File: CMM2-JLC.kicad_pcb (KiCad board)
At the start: 4 copper layers, 130 x 102 mm, 111 parts, among them J1 Nunchuck, J2 VGA, J3 EXTERNAL I/O, J4 USB_C_Receptacle_USB2.0, J5 Audio, J6 USB A Host, J7 SWD, J8 Micro_SD_Card_Det, J9 Boot select, SW1 Reset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

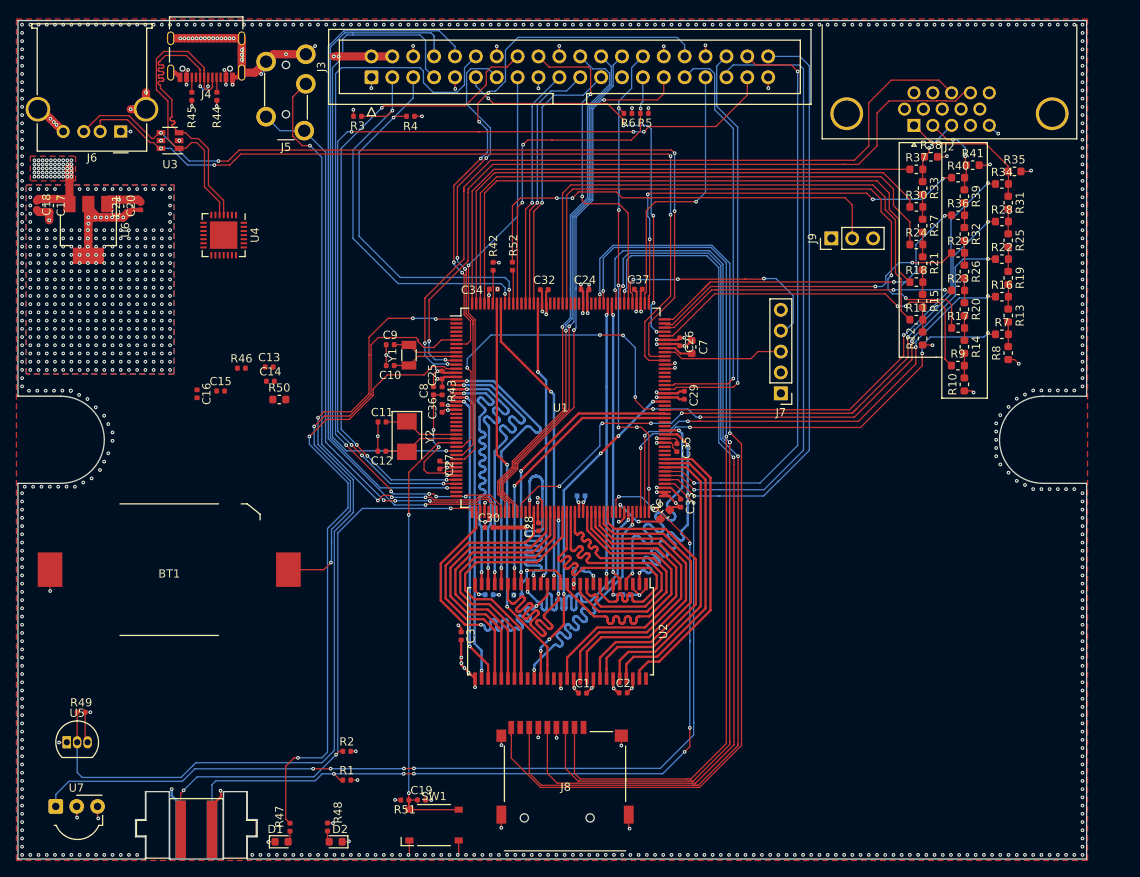
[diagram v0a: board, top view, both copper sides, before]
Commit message: Routed USB, UART and reset pins
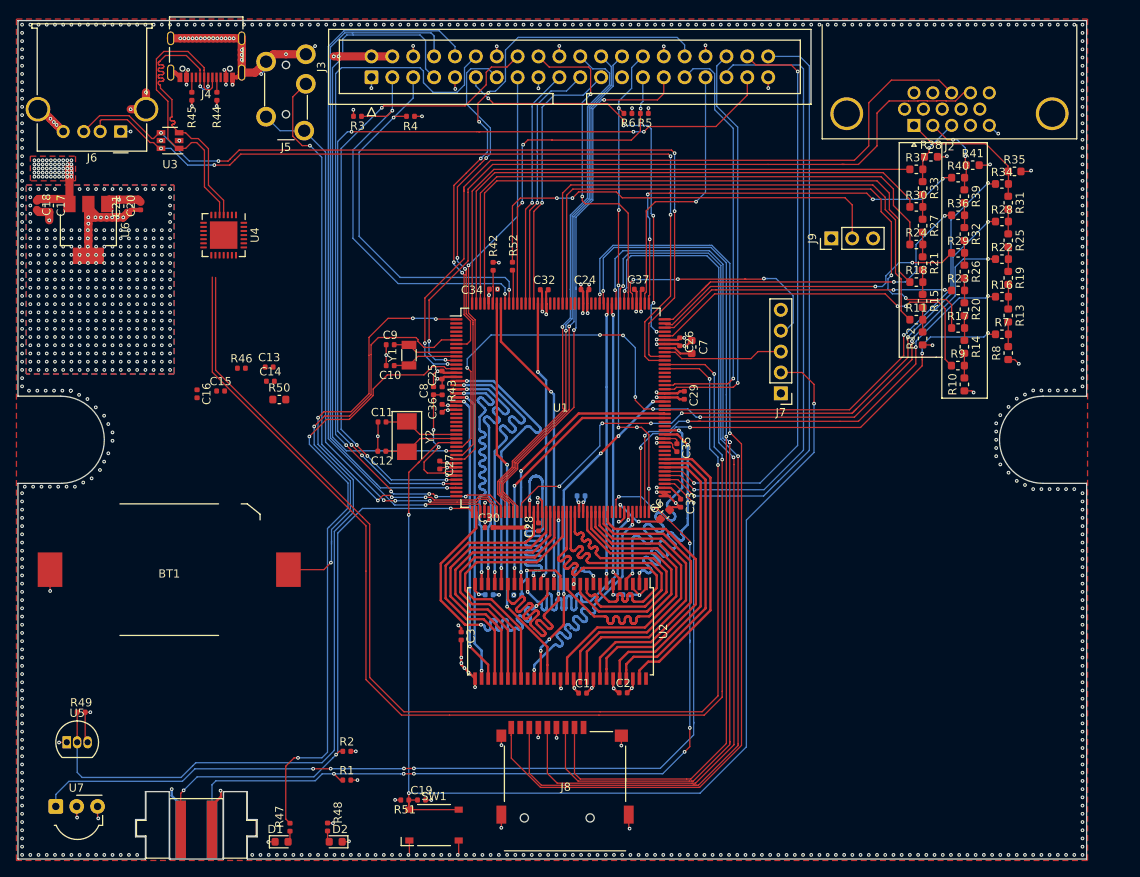
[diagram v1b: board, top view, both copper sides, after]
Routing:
- net /PA10: track 1.32 -> 149.0 mm, vias 1 -> 2
- net /PA9: track 1.30 -> 146.3 mm, vias 1 -> 2
- net /RESET: track 56.5 -> 152.2 mm, vias 2 -> 3
- net /PI1: track 43.9 -> 43.2 mm
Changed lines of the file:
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@@
     (thickness 1.6)
     (drawings 44)
-    (tracks 5255)
+    (tracks 5295)
     (zones 0)
     (modules 111)
@@
   (segment (start 133.552998 61.976) (end 132.788499 61.211501) (width 0.127) (layer F.Cu) (net 24))
   (segment (start 133.552999 61.976) (end 133.552998 61.976) (width 0.127) (layer F.Cu) (net 24))
-  (segment (start 132.788499 61.211501) (end 132.75 61.173001) (width 0.127) (layer F.Cu) (net 24))
   (segment (start 128.48851 54.26149) (end 128 54.75) (width 0.127) (layer F.Cu) (net 24))
   (segment (start 128 54.75) (end 127 54.75) (width 0.127) (layer B.Cu) (net 24))
@@
   (segment (start 127.95 51.8) (end 127.3 51.8) (width 0.127) (layer B.Cu) (net 107))
   (segment (start 129.25 50.5) (end 127.95 51.8) (width 0.127) (layer B.Cu) (net 107))
-  (segment (start 127.95 51.8) (end 127.5 52.25) (width 0.127) (layer B.Cu) (net 107))
   (segment (start 103.640776 52.390776) (end 103.785562 52.24599) (width 0.127) (layer F.Cu) (net 107))
   (segment (start 103.240776 52.790776) (end 103.640776 52.390776) (width 0.127) (layer F.Cu) (net 107))
@@
   (segment (start 73.612 115.997) (end 67.612 115.997) (width 0.127) (layer F.Cu) (net 148))
   (segment (start 71.144 71.35) (end 73.325 71.35) (width 0.127) (layer F.Cu) (net 148))
-  (segment (start 67.541 74.953) (end 71.144 71.35) (width 0.127) (layer F.Cu) (net 148))
   (segment (start 67.541 115.926) (end 67.612 115.997) (width 0.127) (layer F.Cu) (net 148))
   (segment (start 67.541 80.1219) (end 67.5386 80.1243) (width 0.127) (layer F.Cu) (net 148))
@@
   (segment (start 67.5386 80.1243) (end 67.5386 113.9825) (width 0.127) (layer B.Cu) (net 148))
   (segment (start 67.541 113.9849) (end 67.541 115.926) (width 0.127) (layer F.Cu) (net 148))
+  (segment (start 68.7578 73.7362) (end 68.6816 73.8124) (width 0.127) (layer F.Cu) (net 148))
+  (segment (start 67.541 74.953) (end 68.7578 73.7362) (width 0.127) (layer F.Cu) (net 148))
+  (segment (start 68.7578 73.7362) (end 71.144 71.35) (width 0.127) (layer F.Cu) (net 148))
+  (segment (start 112.8 62.81) (end 115.388 62.81) (width 0.127) (layer F.Cu) (net 148))
+  (via (at 116.84 66.5988) (size 0.45) (drill 0.2) (layers F.Cu B.Cu) (net 148))
+  (segment (start 116.84 64.262) (end 116.84 66.5988) (width 0.127) (layer F.Cu) (net 148))
+  (segment (start 115.388 62.81) (end 116.84 64.262) (width 0.127) (layer F.Cu) (net 148))
+  (segment (start 116.84 66.5988) (end 116.84 72.5424) (width 0.127) (layer B.Cu) (net 148))
+  (segment (start 116.84 72.5424) (end 108.6104 80.772) (width 0.127) (layer B.Cu) (net 148))
+  (segment (start 108.6104 80.772) (end 108.6104 108.3564) (width 0.127) (layer B.Cu) (net 148))
+  (segment (start 102.9819 113.9849) (end 108.6104 108.3564) (width 0.127) (layer B.Cu) (net 148))
+  (segment (start 67.541 113.9849) (end 102.9819 113.9849) (width 0.127) (layer B.Cu) (net 148))
   (segment (start 53.086 119.6755) (end 52.8575 119.904) (width 0.127) (layer F.Cu) (net 149))
   (segment (start 53.086 118.611) (end 53.086 119.6755) (width 0.127) (layer F.Cu) (net 149))
@@
   (segment (start 41.15 28.723) (end 41.148 28.725) (width 0.127) (layer F.Cu) (net 158))
   (segment (start 41.15 26.91) (end 41.15 28.723) (width 0.127) (layer F.Cu) (net 158))
-  (via (at 99.921751 61.666754) (size 0.45) (drill 0.2) (layers F.Cu B.Cu) (net 161))
-  (segment (start 99.738505 61.85) (end 99.921751 61.666754) (width 0.127) (layer F.Cu) (net 161))
-  (segment (start 98.675 61.85) (end 99.738505 61.85) (width 0.127) (layer F.Cu) (net 161))
+  (segment (start 98.675 61.85) (end 98.7308 61.85) (width 0.127) (layer F.Cu) (net 161))
+  (via (at 105.664 73.406) (size 0.45) (drill 0.2) (layers F.Cu B.Cu) (net 161))
+  (segment (start 105.664 72.8472) (end 105.664 73.406) (width 0.127) (layer B.Cu) (net 161))
+  (segment (start 104.6988 71.882) (end 105.664 72.8472) (width 0.127) (layer B.Cu) (net 161))
+  (segment (start 105.664 101.6) (end 105.664 102.3112) (width 0.127) (layer F.Cu) (net 161))
+  (segment (start 105.664 73.406) (end 105.664 101.6) (width 0.127) (layer F.Cu) (net 161))
+  (segment (start 105.664 102.3112) (end 103.4796 104.4956) (width 0.127) (layer F.Cu) (net 161))
+  (segment (start 103.4796 104.4956) (end 90.678 104.4956) (width 0.127) (layer F.Cu) (net 161))
+  (segment (start 103.5568 61.85) (end 104.6988 62.992) (width 0.127) (layer F.Cu) (net 161))
+  (segment (start 102.998 61.85) (end 103.5568 61.85) (width 0.127) (layer F.Cu) (net 161))
+  (via (at 104.6988 62.992) (size 0.45) (drill 0.2) (layers F.Cu B.Cu) (net 161))
+  (segment (start 104.6988 62.992) (end 104.6988 71.882) (width 0.127) (layer B.Cu) (net 161))
+  (segment (start 98.675 61.85) (end 102.998 61.85) (width 0.127) (layer F.Cu) (net 161))
+  (segment (start 90.678 104.4956) (end 72.4916 104.4956) (width 0.127) (layer F.Cu) (net 161))
+  (segment (start 66.652698 104.4956) (end 62.3316 100.174502) (width 0.127) (layer F.Cu) (net 161))
+  (segment (start 72.4916 104.4956) (end 66.652698 104.4956) (width 0.127) (layer F.Cu) (net 161))
+  (segment (start 62.3316 100.174502) (end 62.3316 86.9696) (width 0.127) (layer F.Cu) (net 161))
+  (segment (start 62.3316 81.46358) (end 43.6372 62.76918) (width 0.127) (layer F.Cu) (net 161))
+  (segment (start 62.3316 86.9696) (end 62.3316 81.46358) (width 0.127) (layer F.Cu) (net 161))
+  (segment (start 43.6372 62.76918) (end 43.6372 51.2064) (width 0.127) (layer F.Cu) (net 161))
   (segment (start 80.25 50.47) (end 80.15 50.37) (width 0.127) (layer F.Cu) (net 162))
   (segment (start 80.25 54.425) (end 80.25 50.47) (width 0.127) (layer F.Cu) (net 162))
@@
   (segment (start 110.0243 60.27) (end 112.8 60.27) (width 0.127) (layer F.Cu) (net 165))
   (segment (start 109.16339 61.13091) (end 110.0243 60.27) (width 0.127) (layer F.Cu) (net 165))
-  (via (at 99.92689 62.243733) (size 0.45) (drill 0.2) (layers F.Cu B.Cu) (net 166))
-  (segment (start 99.820623 62.35) (end 99.92689 62.243733) (width 0.127) (layer F.Cu) (net 166))
-  (segment (start 98.675 62.35) (end 99.820623 62.35) (width 0.127) (layer F.Cu) (net 166))
+  (via (at 104.14 63.6016) (size 0.45) (drill 0.2) (layers F.Cu B.Cu) (net 166))
+  (segment (start 102.8884 62.35) (end 104.14 63.6016) (width 0.127) (layer F.Cu) (net 166))
+  (segment (start 98.675 62.35) (end 102.8884 62.35) (width 0.127) (layer F.Cu) (net 166))
+  (segment (start 104.14 63.6016) (end 104.14 72.0852) (width 0.127) (layer B.Cu) (net 166))
+  (via (at 105.156 74.0664) (size 0.45) (drill 0.2) (layers F.Cu B.Cu) (net 166))
+  (segment (start 105.156 73.1012) (end 105.156 74.0664) (width 0.127) (layer B.Cu) (net 166))
+  (segment (start 104.14 72.0852) (end 105.156 73.1012) (width 0.127) (layer B.Cu) (net 166))
+  (segment (start 105.156 74.0664) (end 105.156 102.1588) (width 0.127) (layer F.Cu) (net 166))
+  (segment (start 105.156 102.1588) (end 103.2256 104.0892) (width 0.127) (layer F.Cu) (net 166))
+  (segment (start 103.2256 104.0892) (end 90.8304 104.0892) (width 0.127) (layer F.Cu) (net 166))
+  (segment (start 90.8304 104.0892) (end 66.9544 104.0892) (width 0.127) (layer F.Cu) (net 166))
+  (segment (start 62.7888 99.9236) (end 62.7888 81.28) (width 0.127) (layer F.Cu) (net 166))
+  (segment (start 66.9544 104.0892) (end 62.7888 99.9236) (width 0.127) (layer F.Cu) (net 166))
+  (segment (start 62.7888 81.28) (end 61.9252 80.4164) (width 0.127) (layer F.Cu) (net 166))
+  (segment (start 61.9252 80.4164) (end 49.4792 67.9704) (width 0.127) (layer F.Cu) (net 166))
+  (segment (start 49.4792 67.9704) (end 44.0436 62.5348) (width 0.127) (layer F.Cu) (net 166))
+  (segment (start 44.0436 62.5348) (end 44.0436 51.2572) (width 0.127) (layer F.Cu) (net 166))
   (segment (start 80.173991 73.570111) (end 81.507551 72.236551) (width 0.09) (layer F.Cu) (net 168))
   (segment (start 80.137 73.607102) (end 80.173991 73.570111) (width 0.09) (layer F.Cu) (net 168))

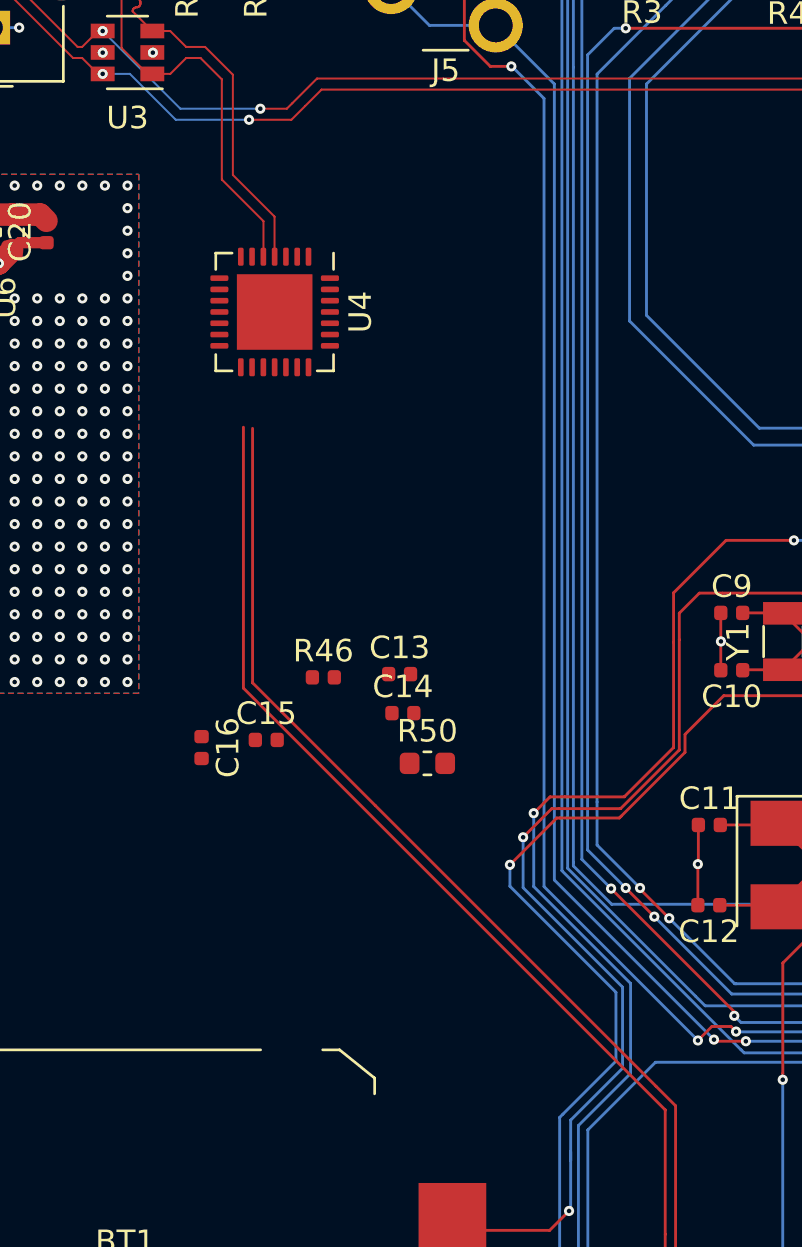
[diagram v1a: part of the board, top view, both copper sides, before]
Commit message: Add CP2102 routing
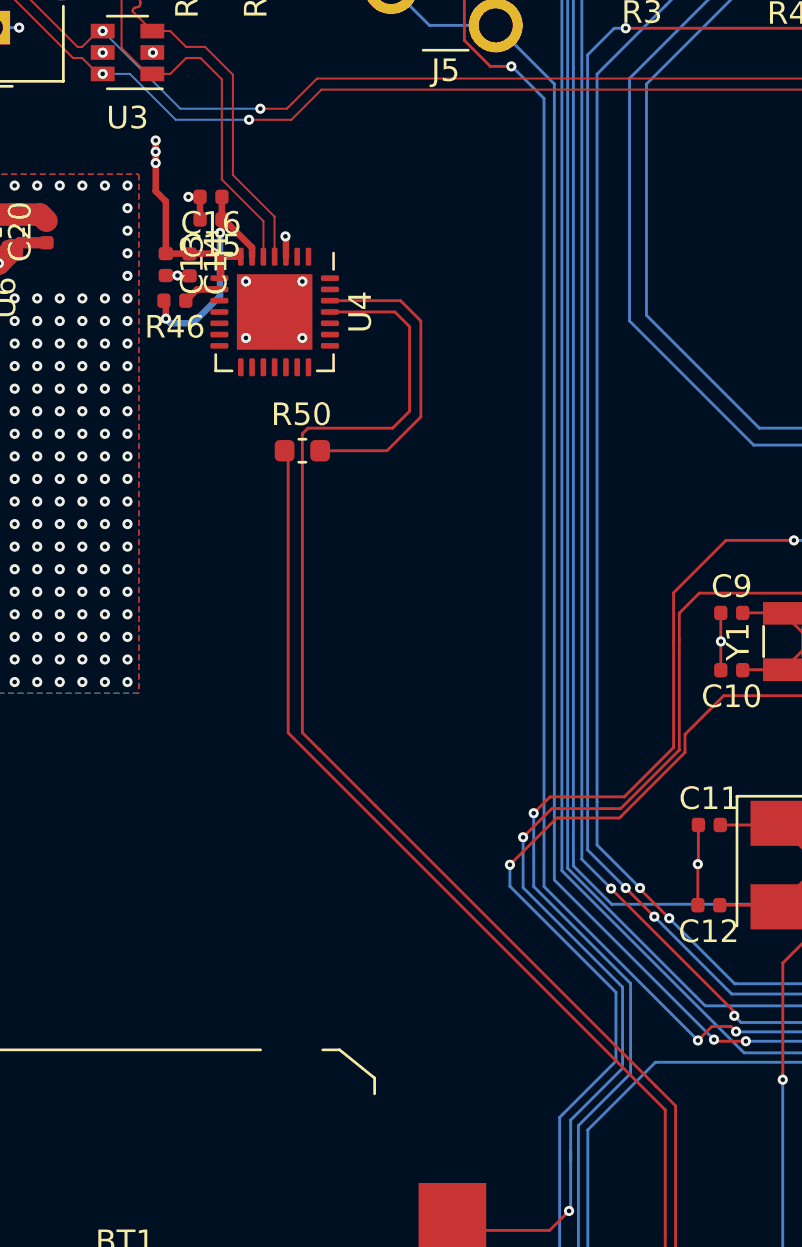
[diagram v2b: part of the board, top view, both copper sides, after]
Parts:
- moved C16 24.4 mm to (42.2, 41.0), turned to 180 degrees
- moved C15 23.2 mm to (42.2, 42.0), turned to 180 degrees
- moved C14 22.0 mm to (41.2, 44.0), turned to 270 degrees
- moved C13 20.9 mm to (40.2, 44.0), turned to 270 degrees
- moved R46 17.9 mm to (40.6, 45.6), turned to 180 degrees
- moved R50 14.9 mm to (46.2, 52.2)
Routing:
- net Net-(R50-Pad2): track 0.00 -> 13.7 mm
- net /PA9: track 146.3 -> 157.8 mm
- net Net-(C15-Pad1): track 0.00 -> 10.6 mm, vias 0 -> 2
- net +5V: track 21.0 -> 30.5 mm, vias 58 -> 61
- net GND: track 158.9 -> 162.4 mm, vias 563 -> 570
- net /PA10: track 149.0 -> 147.2 mm
- net Net-(R46-Pad1): track 0.00 -> 1.74 mm

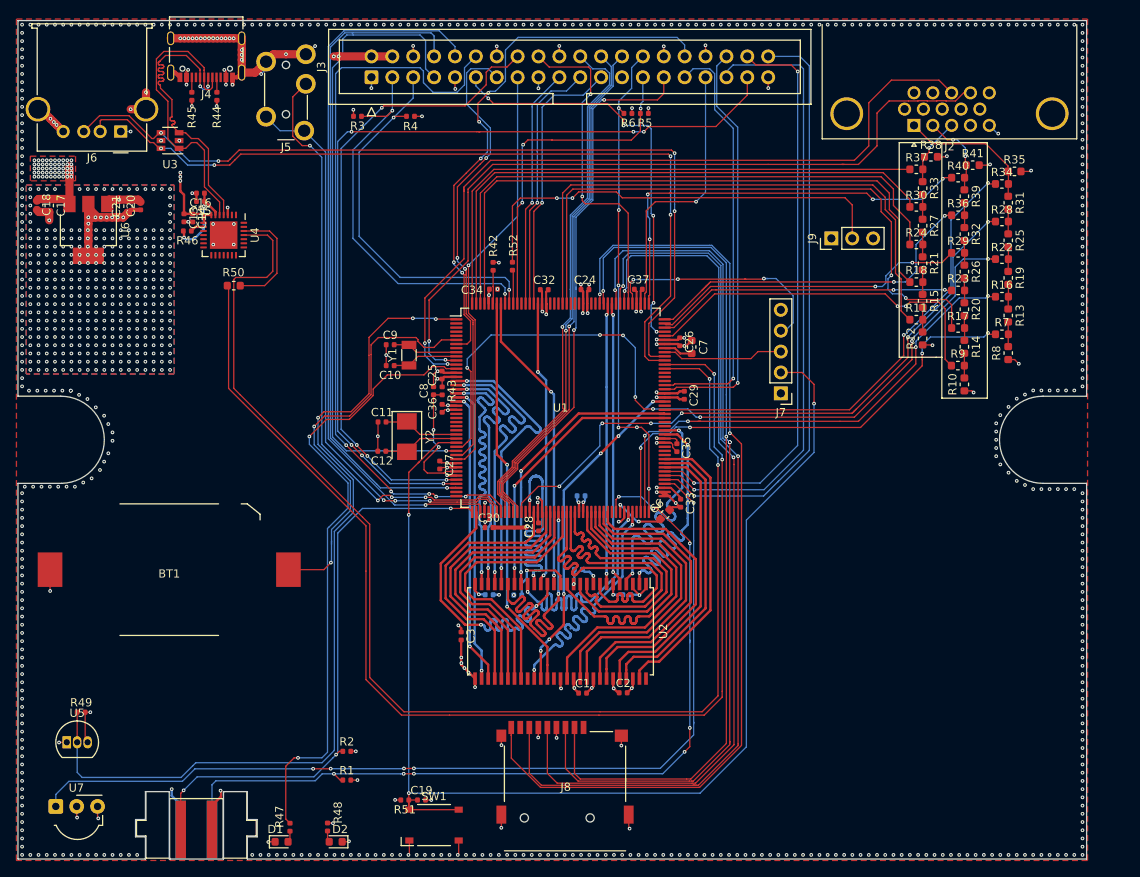
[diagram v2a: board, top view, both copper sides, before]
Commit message: Cleanup silkscreen, add credits
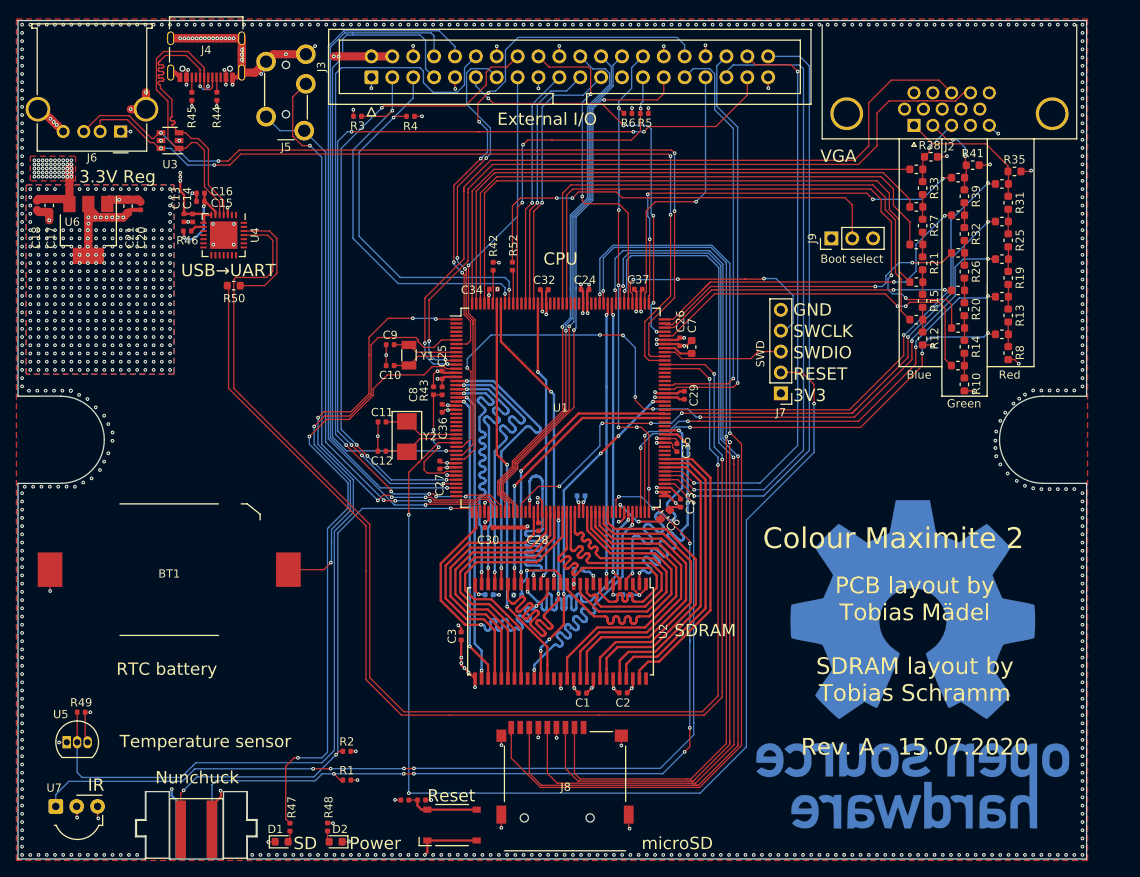
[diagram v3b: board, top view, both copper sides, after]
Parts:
- added REF**: OSHW-Logo_38.1x40mm_Copper, Symbol:OSHW-Logo_38.1x40mm_Copper, B.Cu at (128.9, 98.3)
- moved SW1 2.19 mm to (72.8, 117.9)
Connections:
- U3 pad 1: /USB_C_D- -> /USB_C_D+
- U3 pad 3: /USB_C_D+ -> /USB_C_D-
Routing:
- net /PH14: track 51.1 -> 63.9 mm
- net GND: track 162.4 -> 167.2 mm
- net /RESET: track 152.2 -> 151.1 mm
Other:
- board text added: "3.3V Reg"
- board text added: "3V3"
- board text added: "Blue"
- board text added: "CPU"
- board text added: "Colour Maximite 2"
- board text added: "External I/O"
- board text added: "GND"
- board text added: "Green"
- board text added: "IR"
- board text added: "Nunchuck"
- board text added: "PCB layout by Tobias Mädel SDRAM layout by Tobias Schramm Rev. A - 15.07.2020"
- board text added: "Power"
- board text added: "RESET"
- board text added: "RTC battery"
- board text added: "Red"
- board text added: "Reset"
- board text added: "SD"
- board text added: "SDRAM"
- board text added: "SWCLK"
- board text added: "SWDIO"
- board text added: "Temperature sensor"
- board text added: "USB→UART"
- board text added: "VGA"
- board text added: "microSD"
- board text added: "tbspace.de"

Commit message: Add pin1 markers and revA gerbers
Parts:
- removed the REF** at (128.9, 98.3)
- added REF**: OSHW-Logo_38.1x40mm_SilkScreen, Symbol:OSHW-Logo_38.1x40mm_SilkScreen, B.Cu at (129.3, 98.3)
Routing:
- added copper zone on B.Cu, net GND
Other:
- board text added: "JLCJLCJLCJLC"
